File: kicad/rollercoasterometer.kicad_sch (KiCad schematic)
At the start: 16 parts, among them J101 USB_C_Receptacle, J120 STANDOFF, J125 STANDOFF, J127 STANDOFF, J129 STANDOFF, U104 Teensy4.1, U105 TeensyView

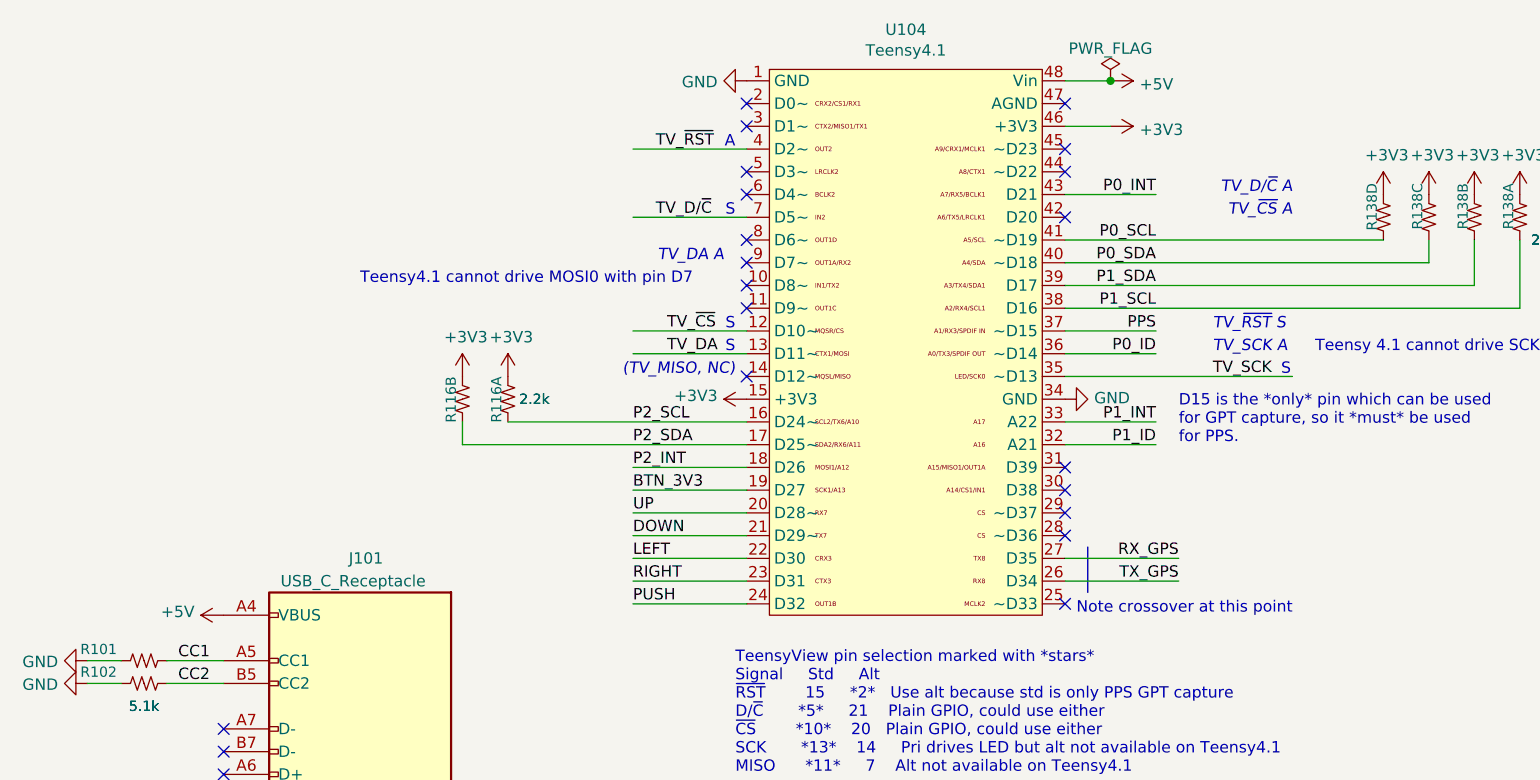
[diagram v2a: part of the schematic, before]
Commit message: Moved USB+ connectors to bottom of board
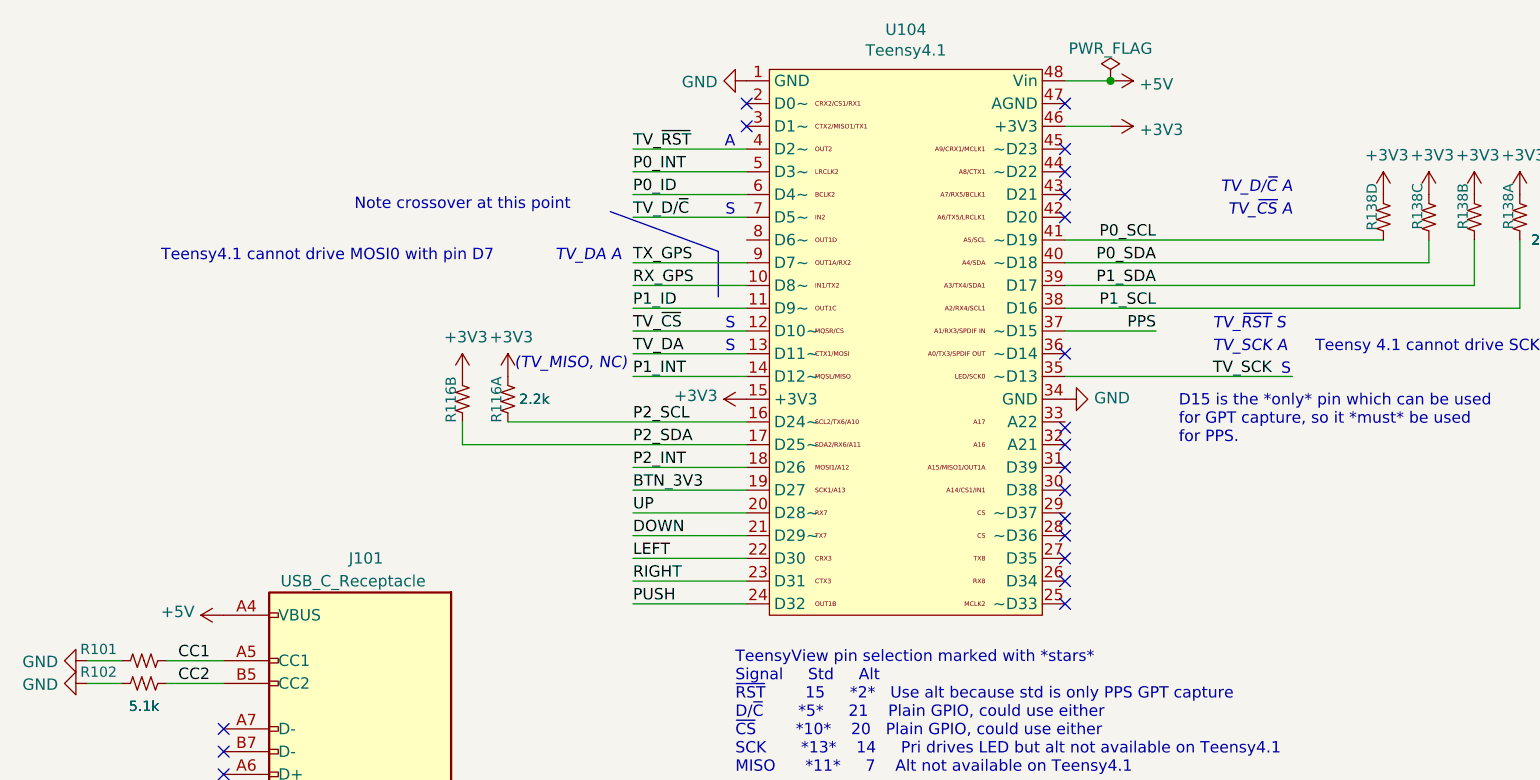
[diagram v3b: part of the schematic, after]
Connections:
- net P0_ID: now also U104.6 (D4~); no longer U104.36 (~D14)
- net P0_INT: now also U104.5 (D3~); no longer U104.43 (D21)
- net P1_ID: now also U104.11 (D9~); no longer U104.32 (A21)
- net P1_INT: now also U104.14 (D12~); no longer U104.33 (A22)
- net RX_GPS: now also U104.10 (D8~); no longer U104.27 (D35)
- net TX_GPS: now also U104.9 (D7~); no longer U104.26 (D34)
- no-connect marks 55 -> 54
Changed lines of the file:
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@@
   (junction (at 215.9 20.32) (diameter 0) (color 0 0 0 0)
   )
-  (no_connect (at 210.82 68.58))
-  (no_connect (at 175.26 33.02))
   (no_connect (at 210.82 22.86))
   (no_connect (at 116.84 115.57))
-  (no_connect (at 175.26 43.18))
-  (no_connect (at 175.26 25.4))
+  (no_connect (at 210.82 71.12))
+  (no_connect (at 210.82 73.66))
+  (no_connect (at 210.82 76.2))
+  (no_connect (at 210.82 78.74))
+  (no_connect (at 210.82 59.055))
+  (no_connect (at 210.82 60.96))
+  (no_connect (at 210.82 63.5))
+  (no_connect (at 210.82 66.04))
+  (no_connect (at 210.82 69.215))
   (no_connect (at 236.22 110.49))
   (no_connect (at 236.22 113.03))
@@
   (no_connect (at 50.8 66.04))
   (no_connect (at 116.84 95.25))
-  (no_connect (at 210.82 66.04))
-  (no_connect (at 175.26 22.86))
-  (no_connect (at 175.26 40.64))
-  (no_connect (at 175.26 30.48))
-  (no_connect (at 175.26 53.34))
-  (no_connect (at 210.82 78.74))
-  (no_connect (at 175.26 45.72))
-  (no_connect (at 210.82 35.56))
-  (no_connect (at 210.82 71.12))
-  (no_connect (at 210.82 63.5))
+  (no_connect (at 210.82 50.8))
   (no_connect (at 50.8 27.94))
   (no_connect (at 210.82 27.94))
+  (no_connect (at 175.26 25.4))
+  (no_connect (at 175.26 22.86))
+  (no_connect (at 210.82 33.02))
+  (no_connect (at 210.82 35.56))
   (no_connect (at 116.84 100.33))
   (no_connect (at 116.84 92.71))
@@
   (no_connect (at 116.84 138.43))
   (no_connect (at 210.82 30.48))
-  (no_connect (at 175.26 38.1))
   (wire (pts (xy 210.82 53.34) (xy 236.22 53.34))
     (stroke (width 0) (type default) (color 0 0 0 0))
@@
     (stroke (width 0) (type default) (color 0 0 0 0))
   )
-  (polyline (pts (xy 213.36 72.39) (xy 213.36 77.47))
+  (polyline (pts (xy 172.085 39.37) (xy 172.085 44.45))
     (stroke (width 0) (type default) (color 0 0 0 0))
   )
@@
     (stroke (width 0) (type default) (color 0 0 0 0))
   )
-  (wire (pts (xy 210.82 33.02) (xy 220.98 33.02))
-    (stroke (width 0) (type default) (color 0 0 0 0))
-  )
-  (wire (pts (xy 223.52 76.2) (xy 210.82 76.2))
+  (wire (pts (xy 162.56 30.48) (xy 175.26 30.48))
+    (stroke (width 0) (type default) (color 0 0 0 0))
+  )
+  (wire (pts (xy 175.26 43.18) (xy 162.56 43.18))
     (stroke (width 0) (type default) (color 0 0 0 0))
   )
@@
     (stroke (width 0) (type default) (color 0 0 0 0))
   )
-  (wire (pts (xy 223.52 73.66) (xy 210.82 73.66))
+  (wire (pts (xy 175.26 40.64) (xy 162.56 40.64))
     (stroke (width 0) (type default) (color 0 0 0 0))
   )
@@
     (stroke (width 0) (type default) (color 0 0 0 0))
   )
-  (wire (pts (xy 220.98 58.42) (xy 210.82 58.42))
+  (wire (pts (xy 162.56 53.34) (xy 175.26 53.34))
     (stroke (width 0) (type default) (color 0 0 0 0))
   )
@@
     (stroke (width 0) (type default) (color 0 0 0 0))
   )
+  (polyline (pts (xy 160.02 34.925) (xy 172.085 39.37))
+    (stroke (width 0) (type default) (color 0 0 0 0))
+  )
   (wire (pts (xy 210.82 38.1) (xy 246.38 38.1))
     (stroke (width 0) (type default) (color 0 0 0 0))
@@
     (stroke (width 0) (type default) (color 0 0 0 0))
   )
-  (wire (pts (xy 220.98 50.8) (xy 210.82 50.8))
+  (wire (pts (xy 162.56 33.02) (xy 175.26 33.02))
     (stroke (width 0) (type default) (color 0 0 0 0))
   )
@@
     (stroke (width 0) (type default) (color 0 0 0 0))
   )
-  (wire (pts (xy 220.98 60.96) (xy 210.82 60.96))
+  (wire (pts (xy 162.56 45.72) (xy 175.26 45.72))
     (stroke (width 0) (type default) (color 0 0 0 0))
   )
@@
     (effects (font (size 1.27 1.27)) (justify left bottom))
   )
-  (text "(TV_MISO, NC)" (at 173.99 53.34 180)
+  (text "(TV_MISO, NC)" (at 161.925 52.705 180)
     (effects (font (size 1.27 1.27) italic) (justify right bottom))
   )
@@
     (effects (font (size 1.27 1.27) italic) (justify right bottom))
   )
-  (text "Teensy4.1 cannot drive MOSI0 with pin D7" (at 132.08 43.18 0)
+  (text "Teensy4.1 cannot drive MOSI0 with pin D7" (at 109.855 40.64 0)
     (effects (font (size 1.27 1.27)) (justify left bottom))
   )
@@
     (effects (font (size 1.27 1.27)) (justify left bottom))
   )
-  (text "Note crossover at this point" (at 212.09 80.01 0)
-    (effects (font (size 1.27 1.27)) (justify left bottom))
-  )
-  (text "TV_DA A\n" (at 172.72 40.64 180)
+  (text "Note crossover at this point" (at 131.445 34.925 0)
+    (effects (font (size 1.27 1.27)) (justify left bottom))
+  )
+  (text "TV_DA A\n" (at 161.29 40.64 180)
     (effects (font (size 1.27 1.27) italic) (justify right bottom))
   )
@@
     (effects (font (size 1.27 1.27)) (justify left bottom))
   )
-  (label "P1_INT" (at 220.98 58.42 180)
-    (effects (font (size 1.27 1.27)) (justify right bottom))
+  (label "P1_INT" (at 162.56 53.34 0)
+    (effects (font (size 1.27 1.27)) (justify left bottom))
   )
   (label "CC2" (at 111.76 87.63 0)
@@
     (effects (font (size 1.27 1.27)) (justify left bottom))
   )
-  (label "P1_ID" (at 220.98 60.96 180)
-    (effects (font (size 1.27 1.27)) (justify right bottom))
+  (label "P1_ID" (at 162.56 45.72 0)
+    (effects (font (size 1.27 1.27)) (justify left bottom))
   )
   (label "PUSH" (at 215.9 124.46 180)
@@
     (effects (font (size 1.27 1.27)) (justify right bottom))
   )
-  (label "TV_DA" (at 166.37 50.8 0)
+  (label "TV_DA" (at 162.56 50.8 0)
     (effects (font (size 1.27 1.27)) (justify left bottom))
   )
@@
     (effects (font (size 1.27 1.27)) (justify left bottom))
   )
-  (label "P0_INT" (at 220.98 33.02 180)
-    (effects (font (size 1.27 1.27)) (justify right bottom))
+  (label "P0_INT" (at 162.56 30.48 0)
+    (effects (font (size 1.27 1.27)) (justify left bottom))
   )
   (label "TV_~{CS}" (at 224.79 135.89 0)
@@
     (effects (font (size 1.27 1.27)) (justify left bottom))
   )
-  (label "TV_D{slash}~{C}" (at 165.1 35.56 0)
+  (label "TV_D{slash}~{C}" (at 162.56 35.56 0)
     (effects (font (size 1.27 1.27)) (justify left bottom))
   )
@@
     (effects (font (size 1.27 1.27)) (justify right bottom))
   )
-  (label "TV_~{CS}" (at 166.37 48.26 0)
+  (label "TV_~{CS}" (at 162.56 48.26 0)
     (effects (font (size 1.27 1.27)) (justify left bottom))
   )
@@
     (effects (font (size 1.27 1.27)) (justify right bottom))
   )
-  (label "TX_GPS" (at 223.52 76.2 180)
-    (effects (font (size 1.27 1.27)) (justify right bottom))
+  (label "TX_GPS" (at 162.56 40.64 0)
+    (effects (font (size 1.27 1.27)) (justify left bottom))
   )
   (label "TV_~{RST}" (at 224.79 115.57 0)
@@
     (effects (font (size 1.27 1.27)) (justify right bottom))
   )
-  (label "RX_GPS" (at 223.52 73.66 180)
-    (effects (font (size 1.27 1.27)) (justify right bottom))
-  )
-  (label "P0_ID" (at 220.98 50.8 180)
-    (effects (font (size 1.27 1.27)) (justify right bottom))
+  (label "RX_GPS" (at 162.56 43.18 0)
+    (effects (font (size 1.27 1.27)) (justify left bottom))
+  )
+  (label "P0_ID" (at 162.56 33.02 0)
+    (effects (font (size 1.27 1.27)) (justify left bottom))
   )
   (label "P1_INT" (at 63.5 25.4 180)
@@
     (effects (font (size 1.27 1.27)) (justify left bottom))
   )
-  (label "TV_~{RST}" (at 165.1 27.94 0)
+  (label "TV_~{RST}" (at 162.56 27.94 0)
     (effects (font (size 1.27 1.27)) (justify left bottom))
   )
@@
       (reference "G1505") (unit 1) (value "Axis") (footprint "KwanSystems:Axis")
     )
+    (path "/2faa4796-f6bd-4ac2-85c9-699e2ddc070c/f02c28c7-3f38-4e89-a5a5-1afe4320fda1"
+      (reference "G3502") (unit 1) (value "KwanSystems") (footprint "KwanSystems:StKwansSoldermask")
+    )
+    (path "/2faa4796-f6bd-4ac2-85c9-699e2ddc070c/df52a165-e152-4b4b-9723-7d707d8d8d83"
+      (reference "G3503") (unit 1) (value "DesignedWithKicad") (footprint "KwanSystems:Symbol_KiCAD-Logo_CopperAndSilkScreenTop_small")
+    )
+    (path "/2faa4796-f6bd-4ac2-85c9-699e2ddc070c/c56a872e-69a6-4ad0-bf20-7cca55b8b85a"
+      (reference "G3504") (unit 1) (value "OSHW") (footprint "KwanSystems:OSHW-Symbol_6.7x6mm_SolderMask")
+    )
     (path "/9b90737a-db7d-4723-891c-914666b2b907"

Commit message: Added a NC to the board
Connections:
- no-connect marks 54 -> 55
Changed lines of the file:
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@@
   (junction (at 215.9 20.32) (diameter 0) (color 0 0 0 0)
   )
+  (no_connect (at 175.26 38.1))
   (no_connect (at 210.82 22.86))
   (no_connect (at 116.84 115.57))

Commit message: Checkin before branch
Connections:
- net P2_INT: now also U104.32 (D40); no longer U104.18 (D26)
- no-connect marks 55 -> 54
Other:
- note added: "GPT1 CAP1 on EMC24(alt4, PSRAM CS ) or B1_05 (alt8, ETH_PHY RXD1) GPT1 CAP2 on EMC23(alt4, NC? ) or B1_06 (alt8, ETH_PHY DV ) GPT2 CAP1 on EMC41(alt1, NC? ) or AD_B1_03 (alt8, A1/D15) GPT2 CAP2 on EMC40(alt1, ESD diode) or AD_B1_04 (alt8, A16/D40)"
- note removed: "D15 is the *only* pin which can be used for GPT capture, so it *must* be used for PPS."
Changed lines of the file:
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@@
   (no_connect (at 210.82 76.2))
   (no_connect (at 210.82 78.74))
-  (no_connect (at 210.82 59.055))
-  (no_connect (at 210.82 60.96))
+  (no_connect (at 210.82 58.42))
   (no_connect (at 210.82 63.5))
   (no_connect (at 210.82 66.04))
-  (no_connect (at 210.82 69.215))
+  (no_connect (at 210.82 68.58))
   (no_connect (at 236.22 110.49))
   (no_connect (at 236.22 113.03))
@@
     (stroke (width 0) (type default) (color 0 0 0 0))
   )
-  (wire (pts (xy 175.26 63.5) (xy 162.56 63.5))
+  (wire (pts (xy 223.52 60.96) (xy 210.82 60.96))
     (stroke (width 0) (type default) (color 0 0 0 0))
   )
@@
     (effects (font (size 1.27 1.27) italic) (justify right bottom))
   )
-  (text "D15 is the *only* pin which can be used\nfor GPT capture, so it *must* be used\nfor PPS."
-    (at 223.52 60.96 0)
+  (text "GPT1 CAP1 on EMC24(alt4, PSRAM CS ) or    B1_05 (alt8, ETH_PHY RXD1)\nGPT1 CAP2 on EMC23(alt4, NC?      ) or    B1_06 (alt8, ETH_PHY DV  )\nGPT2 CAP1 on EMC41(alt1, NC?      ) or AD_B1_03 (alt8, A1/D15)\nGPT2 CAP2 on EMC40(alt1, ESD diode) or AD_B1_04 (alt8, A16/D40)"
+    (at 220.98 73.66 0)
     (effects (font (size 1.27 1.27)) (justify left bottom))
   )
@@
     (effects (font (size 1.27 1.27)) (justify left bottom))
   )
-  (label "P2_INT" (at 162.56 63.5 0)
-    (effects (font (size 1.27 1.27)) (justify left bottom))
+  (label "P2_INT" (at 223.52 60.96 180)
+    (effects (font (size 1.27 1.27)) (justify right bottom))
   )
   (label "P1_ID" (at 162.56 45.72 0)
@@
     )
     (path "/ef3523e1-1944-4a94-ac44-9b4df6bc7d84/7e5f1de1-52e8-4e90-b0e4-67c16a4896ae/9a85dbb6-7de4-4cd4-87e8-b287c692a56b"
-      (reference "J402") (unit 1) (value "SolderJumper_2_Open") (footprint "Jumper:SolderJumper-2_P1.3mm_Open_RoundedPad1.0x1.5mm")
+      (reference "J402") (unit 1) (value "NormallyClosed") (footprint "KwanSystems:SolderJumper-2_P1.3mm_MaskBridged_RoundedPad1.0x1.5mm")
     )
     (path "/261f39eb-fd7b-4638-9e1c-4710f0fb640c/d120ec91-a4e8-4cdb-816e-81c4eae20404/088528ed-9597-4a2f-884e-b077d4d99f3c"
@@
       (reference "R3502") (unit 1) (value "5.1k") (footprint "Resistor_SMD:R_0402_1005Metric")
     )
-    (path "/2faa4796-f6bd-4ac2-85c9-699e2ddc070c/f59f839c-15d4-467c-94d5-aa377ab314ed"
-      (reference "S3501") (unit 1) (value "JS1400") (footprint "KwanSystems:JS1400")
+    (path "/2faa4796-f6bd-4ac2-85c9-699e2ddc070c/bb11793f-b75f-4aaf-9075-1d9956c2187f"
+      (reference "S3501") (unit 1) (value "JS5208") (footprint "KwanSystems:JS5208")
     )
     (path "/6321da49-3889-482b-8552-92945daa3d4c"
